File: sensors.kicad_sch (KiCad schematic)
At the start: 5 parts, among them U4 BMI055

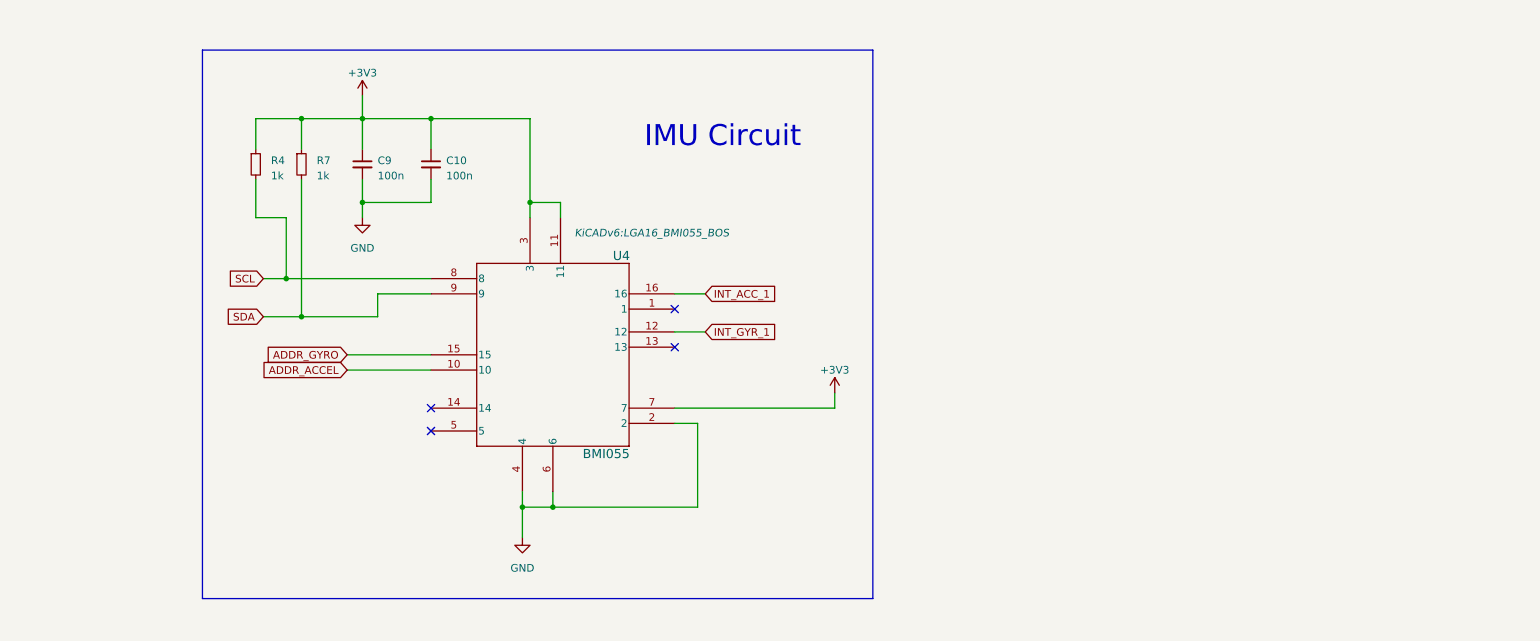
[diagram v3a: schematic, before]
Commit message: Add MPU6050 and LIS2MDL
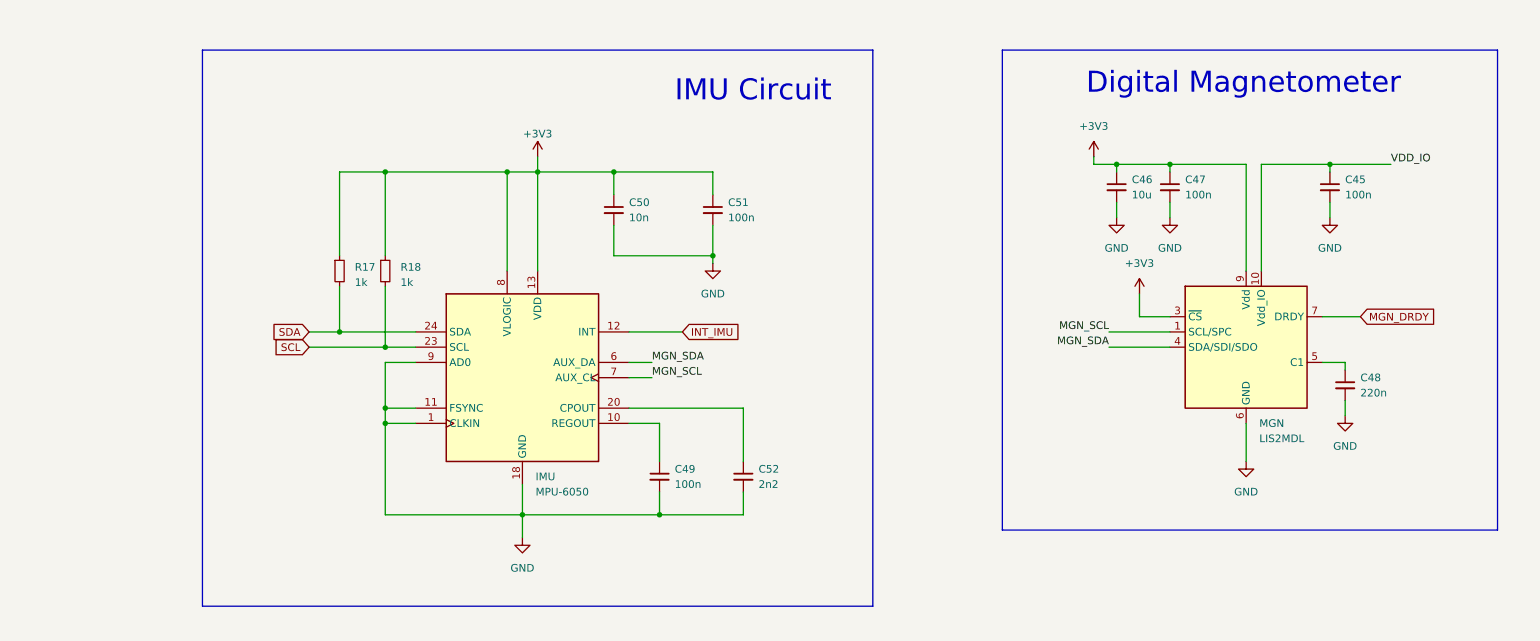
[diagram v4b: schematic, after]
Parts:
- removed C10, C9: 100n, Capacitor_SMD:C_0402_1005Metric, symbol Device:C_Small
- removed R4, R7: 1k, Resistor_SMD:R_0402_1005Metric, symbol Device:R_Small
- removed U4: BMI055, KiCADv6:LGA16_BMI055_BOS, symbol BMI055:BMI055
- added C45, C47, C49, C51: 100n, Capacitor_SMD:C_0402_1005Metric, symbol Device:C_Small
- added C46: 10u, Capacitor_SMD:C_0603_1608Metric, symbol Device:C_Small
- added C48: 220n, Capacitor_SMD:C_0402_1005Metric, symbol Device:C_Small
- added C50: 10n, Capacitor_SMD:C_0402_1005Metric, symbol Device:C_Small
- added C52: 2n2, Capacitor_SMD:C_0402_1005Metric, symbol Device:C_Small
- added IMU: MPU-6050, Sensor_Motion:InvenSense_QFN-24_4x4mm_P0.5mm, symbol Sensor_Motion:MPU-6050
- added MGN: LIS2MDL, Package_LGA:LGA-12_2x2mm_P0.5mm, symbol Sensor_Magnetic:LIS2MDL
- added R17, R18: 1k, Resistor_SMD:R_0402_1005Metric, symbol Device:R_Small
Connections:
- net +3V3: now also C46.1, C47.1, C50.1, C51.1, IMU.13 (VDD), IMU.8 (VLOGIC), MGN.3 (~{CS}), MGN.9 (Vdd), R17.1, R18.1
- net GND: now also C45.2, C46.2, C47.2, C48.2, C49.2, C50.2, C51.2, C52.2, IMU.1 (CLKIN), IMU.11 (FSYNC), IMU.18 (GND), IMU.9 (AD0), MGN.6 (GND), MGN.8 (GND)
- net SCL: now also IMU.23 (SCL), R18.2
- net SDA: now also IMU.24 (SDA), R17.2
- new net: C52.1, IMU.20 (CPOUT)
- new net: C48.1, MGN.5 (C1)
- new net: C49.1, IMU.10 (REGOUT)
- new net INT_IMU: IMU.12 (INT)
- new net MGN_DRDY: MGN.7 (DRDY)
- new net MGN_SCL: IMU.7 (AUX_CL), MGN.1 (SCL/SPC)
- new net MGN_SDA: IMU.6 (AUX_DA), MGN.4 (SDA/SDI/SDO)
- new net VDD_IO: C45.1, MGN.10 (Vdd_IO)
- no-connect marks 4 -> 0
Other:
- note added: "Digital Magnetometer"

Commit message: checkpoint for backup
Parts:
- renumbered IMU to IMU1, MGN to MGN1
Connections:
- net MGN_DRDY is gone; now on net GND: MGN1.7 (DRDY)
- net VDD_IO is gone; now on net +3V3: C45.1, MGN1.10 (Vdd_IO)
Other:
- moved on the sheet: C45, C46, C47, C48, C49, C50, C51, C52, IMU1, MGN1, R17, R18

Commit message: pcb updates & improvements
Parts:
- added JP1: MGN_SCL, Jumper:SolderJumper-3_P2.0mm_Open_TrianglePad1.0x1.5mm, symbol Jumper:SolderJumper_3_Open
- added JP3: MGN_SDA, Jumper:SolderJumper-3_P2.0mm_Open_TrianglePad1.0x1.5mm, symbol Jumper:SolderJumper_3_Open
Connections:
- net MGN_SCL: now also JP1.2 (C); no longer IMU1.7 (AUX_CL)
- net MGN_SDA: now also JP3.2 (C); no longer IMU1.6 (AUX_DA)
- net SCL: now also JP3.1 (A)
- net SDA: now also JP1.1 (A)
- new net MPU_MGN_SCL: IMU1.7 (AUX_CL), JP3.3 (B)
- new net MPU_MGN_SDA: IMU1.6 (AUX_DA), JP1.3 (B)
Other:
- moved on the sheet: C45, C46, C47, C48, C49, C50, C51, C52, IMU1, MGN1, R17, R18
